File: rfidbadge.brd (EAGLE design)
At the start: 93.7 x 48.2 mm, 57 parts, among them Q1 BSS123, U1 ATMEGA328P_TQFP, U2 CLRC663, Y1 27.12 MHz

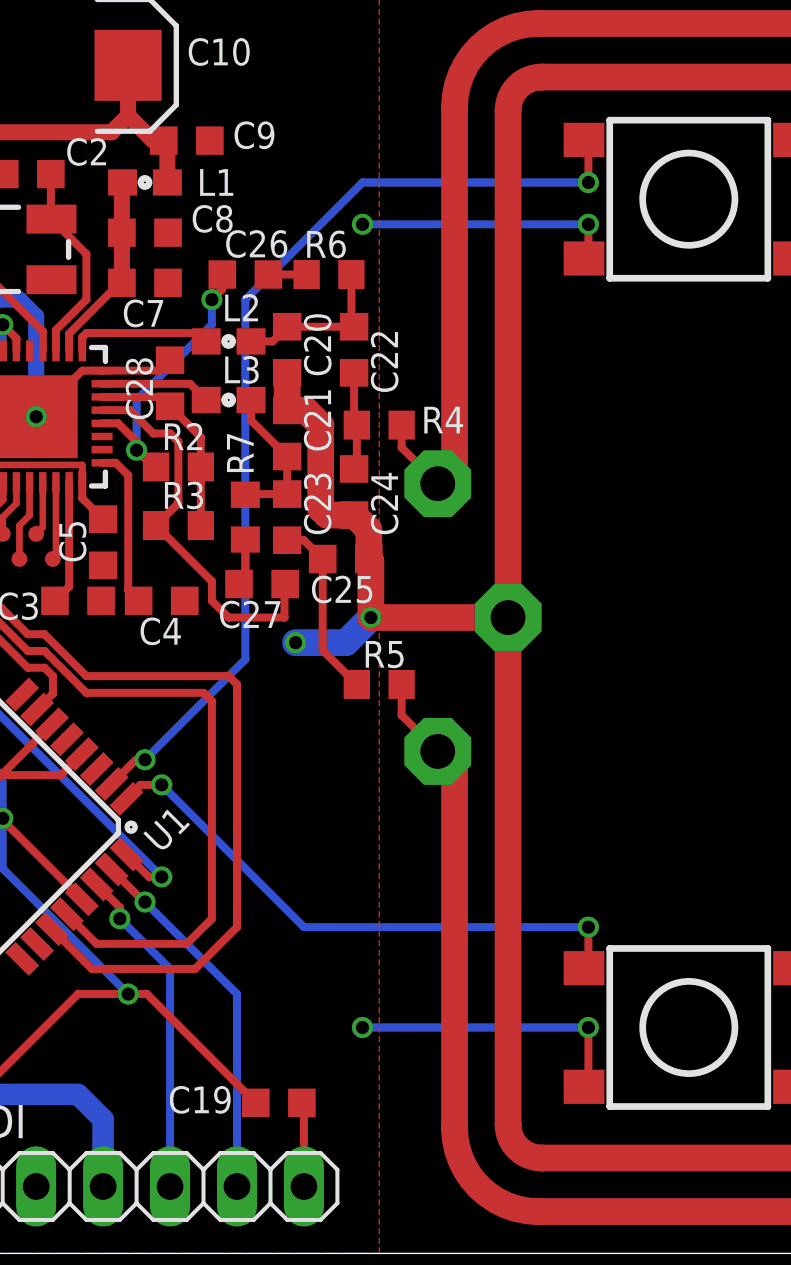
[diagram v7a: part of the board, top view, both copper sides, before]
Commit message: Add reset switch
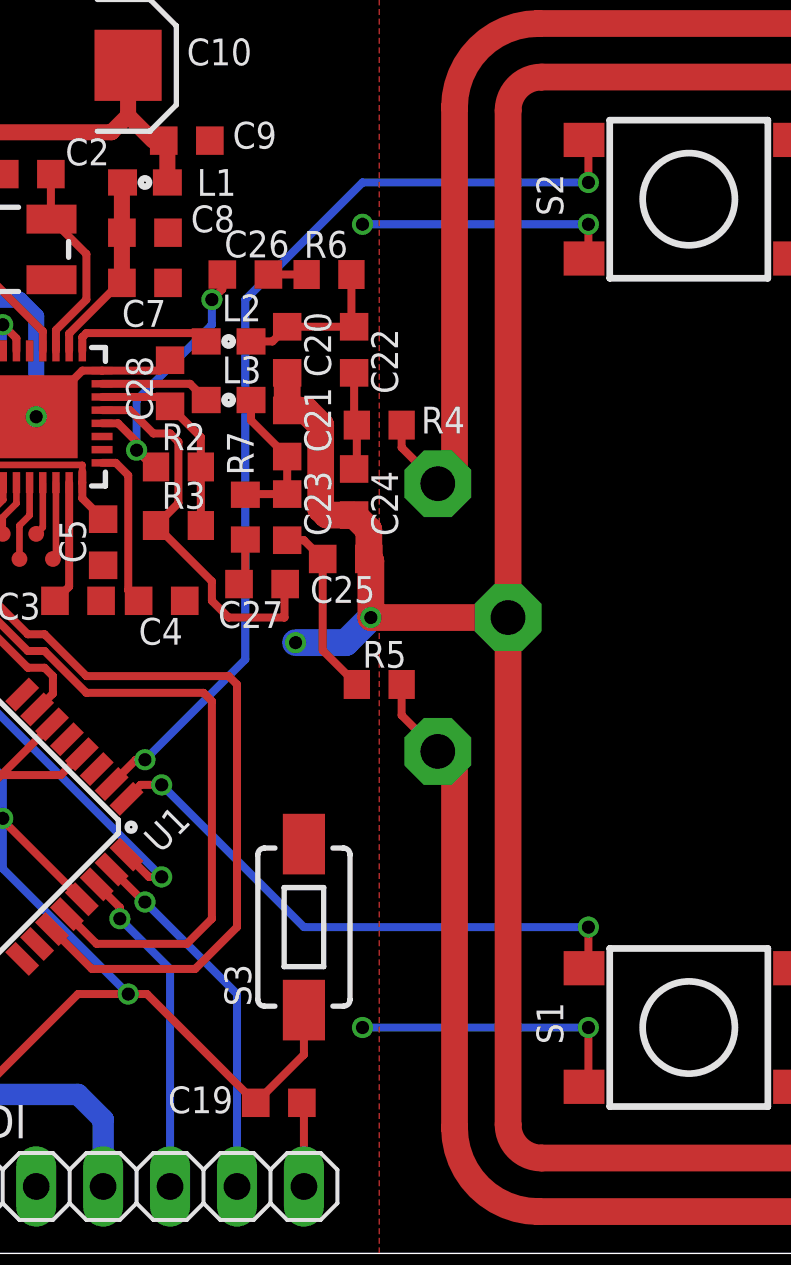
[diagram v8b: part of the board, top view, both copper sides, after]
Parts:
- added S3: RESET, SparkFun-Electromechanical:TACTILE-SWITCH-1101NE
- S1: value SWITCH-MOMENTARY-2SMD-4 -> MENU
- S2: value SWITCH-MOMENTARY-2SMD-4 -> SELECT
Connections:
- net GND: now also S3.2
- net RESET: now also S3.1
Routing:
- net RESET: track 58.0 -> 62.2 mm
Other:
- board text added: "S1"
- board text added: "S2"
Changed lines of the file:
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@@
 <text x="80.01" y="5.08" size="1.778" layer="25" rot="R90">MENU</text>
 <text x="80.01" y="35.2425" size="1.778" layer="25" rot="R90">SELECT</text>
+<text x="66.9925" y="7.9375" size="1.016" layer="25" rot="R90">S1</text>
+<text x="66.9925" y="39.37" size="1.016" layer="25" rot="R90">S2</text>
 </plain>
 <attributes>
@@
 <attribute name="PROD_ID" value="36-2479-ND" x="30.48" y="24.13" size="1.778" layer="28" rot="MR0" display="off"/>
 </element>
-<element name="S1" library="SparkFun-Electromechanical" package="TACTILE_SWITCH_TALL" value="SWITCH-MOMENTARY-2SMD-4" x="71.755" y="8.5725" rot="R180">
+<element name="S1" library="SparkFun-Electromechanical" package="TACTILE_SWITCH_TALL" value="MENU" x="71.755" y="8.5725" rot="R180">
 <attribute name="PROD_ID" value="CKN9112CT-ND" x="71.755" y="8.5725" size="1.778" layer="27" rot="R180" display="off"/>
 </element>
-<element name="S2" library="SparkFun-Electromechanical" package="TACTILE_SWITCH_TALL" value="SWITCH-MOMENTARY-2SMD-4" x="71.755" y="40.005" rot="R180">
+<element name="S2" library="SparkFun-Electromechanical" package="TACTILE_SWITCH_TALL" value="SELECT" x="71.755" y="40.005" rot="R180">
 <attribute name="PROD_ID" value="CKN9112CT-ND" x="71.755" y="40.005" size="1.778" layer="27" rot="R180" display="off"/>
 </element>
@@
 <element name="TP6" library="testpad" package="TP06R" value="TPTP06R" x="47.625" y="26.3525" smashed="yes">
 <attribute name="TP_SIGNAL_NAME" value="" x="47.625" y="24.4475" size="1" layer="37"/>
+</element>
+<element name="S3" library="SparkFun-Electromechanical" package="TACTILE-SWITCH-1101NE" value="RESET" x="57.15" y="12.3825" smashed="yes" rot="R90">
+<attribute name="PROD_ID" value="CKN10388CT-ND" x="57.15" y="12.3825" size="1.778" layer="27" rot="R90" display="off"/>
+<attribute name="NAME" x="55.15" y="9.3825" size="1.016" layer="25" rot="R90"/>
+<attribute name="VALUE" x="61.4375" y="9.3825" size="1.778" layer="27" rot="R90"/>
 </element>
 </elements>
@@
 <wire x1="20.955" y1="24.13" x2="17.78" y2="24.13" width="0.8128" layer="16"/>
 <via x="17.78" y="24.13" extent="1-16" drill="0.5"/>
+<contactref element="S3" pad="2"/>
 </signal>
 <signal name="EXTCLK">
@@
 <wire x1="40.3225" y1="1.5875" x2="48.5775" y2="9.8425" width="0.3048" layer="1"/>
 <wire x1="48.5775" y1="9.8425" x2="50.4825" y2="9.8425" width="0.3048" layer="1"/>
+<contactref element="S3" pad="1"/>
+<wire x1="57.15" y1="9.2325" x2="57.15" y2="7.5425" width="0.3048" layer="1"/>
+<wire x1="57.15" y1="7.5425" x2="55.3225" y2="5.715" width="0.3048" layer="1"/>
 </signal>
 <signal name="CS">
